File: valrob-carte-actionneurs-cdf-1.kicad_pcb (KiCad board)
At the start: 4 copper layers, 50 x 50 mm, 126 parts, among them J1 USB_C_Receptacle_USB2.0_14P, J2 Conn_01x02, J3 Conn_01x02, J4 Conn_01x04_Pin, J5 Conn_01x02, J6 Conn_01x02, J7 Conn_01x12, M1 Motor_Servo, M10 Motor_Servo, M11 Motor_Servo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

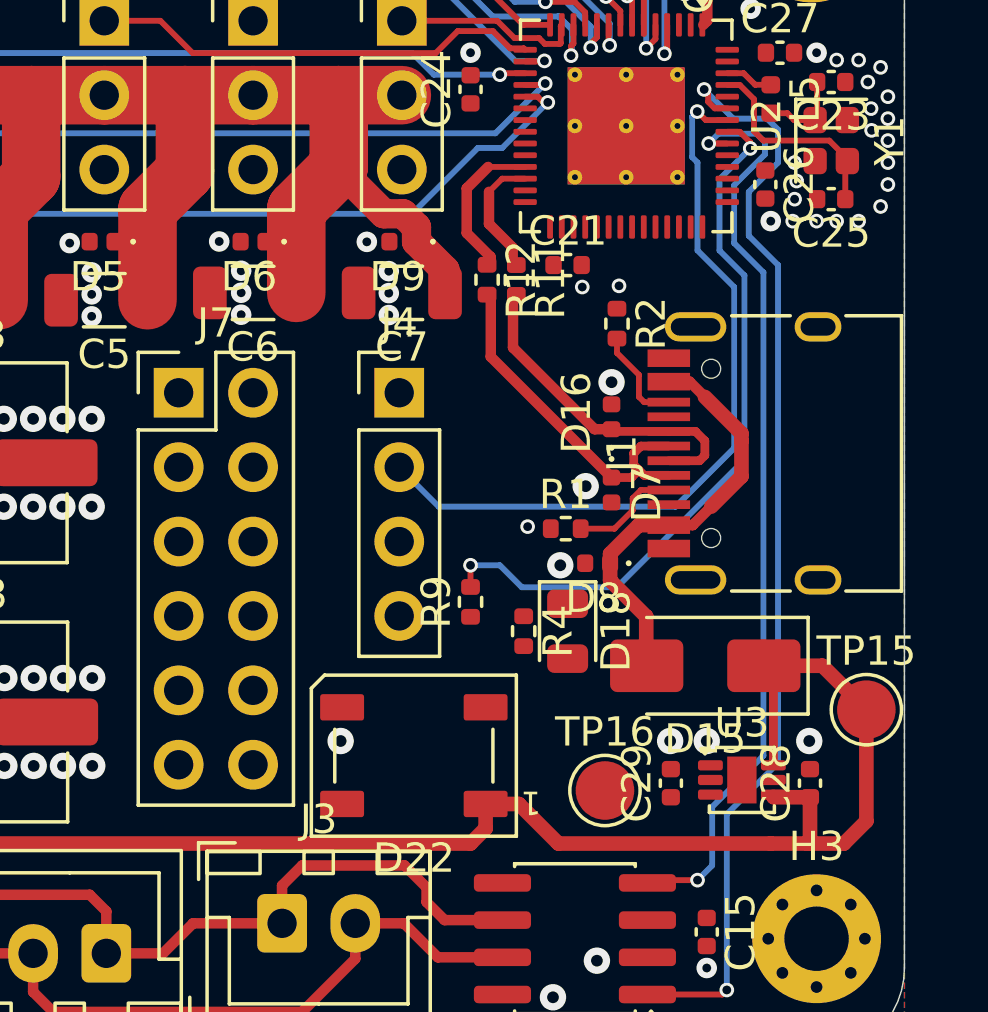
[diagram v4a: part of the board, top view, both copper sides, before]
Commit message: pcb: add spare GPIOs routing
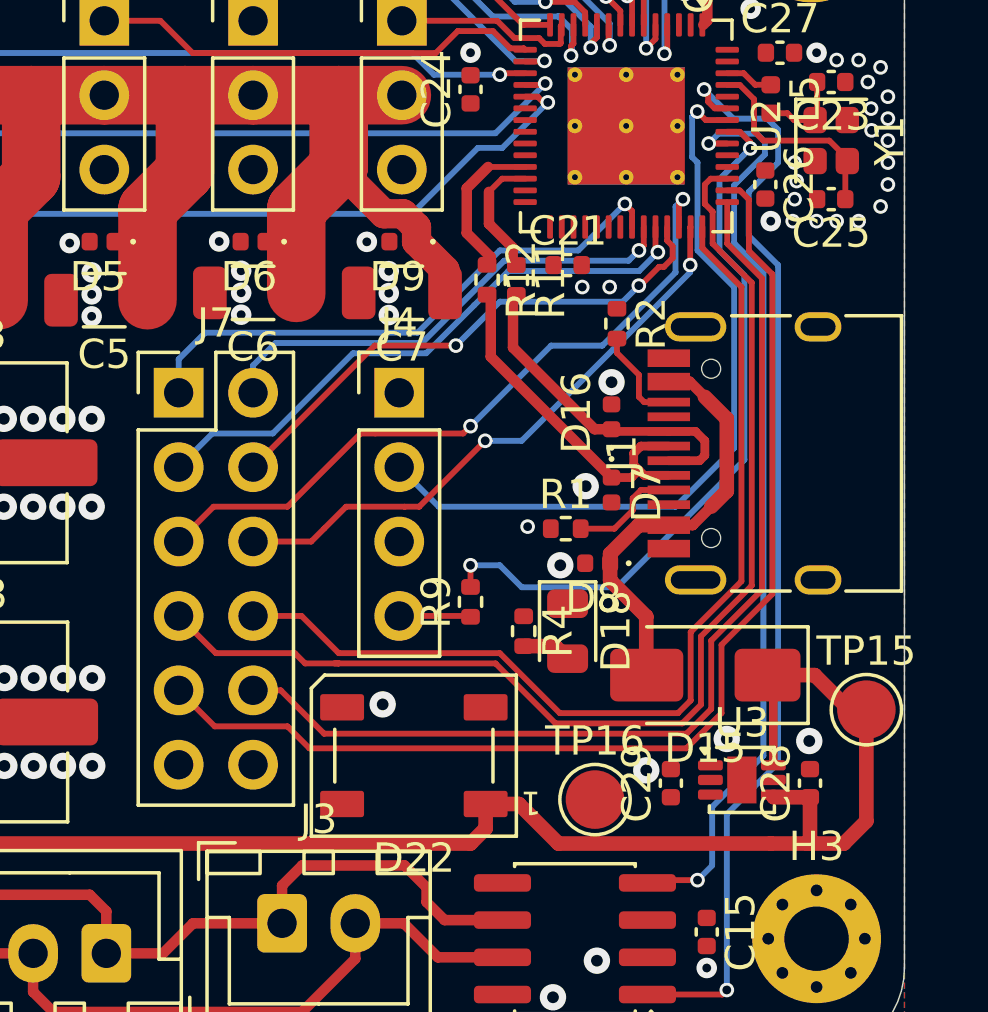
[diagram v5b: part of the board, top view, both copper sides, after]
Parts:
- moved TP16 0.46 mm to (123.4, 100.2)
- moved D15 0.32 mm to (127.2, 96.0)
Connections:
- J7 pad 10: /GPIO40 -> /GPIO38
- J7 pad 11: /GPIO41 -> +3V3
- J7 pad 7: /GPIO37 -> /GPIO40
- J7 pad 8: /GPIO38 -> /GPIO37
- U2 pad 47: /GPIO41 -> unconnected-(U2-MTDI/JTAG/GPIO41-Pad47)
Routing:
- net /GPIO40: track 0.00 -> 39.8 mm
- net /GPIO39: track 0.00 -> 39.3 mm
- net /GPIO38: track 0.00 -> 35.1 mm
- net /GPIO37: track 0.00 -> 33.9 mm
- net /GPIO35: track 0.00 -> 24.4 mm, vias 0 -> 2
- net /GPIO33: track 0.00 -> 20.3 mm, vias 0 -> 1
- net /GPIO36: track 0.00 -> 20.3 mm, vias 0 -> 2
- net /GPIO48: track 0.00 -> 19.5 mm, vias 0 -> 1
- net /GPIO34: track 0.00 -> 18.4 mm, vias 0 -> 2
- net /GPIO47: track 0.00 -> 16.6 mm, vias 0 -> 1
- net Net-(J4-Pin_4): track 0.00 -> 2.45 mm
- net Net-(D18-A): track 0.00 -> 1.68 mm

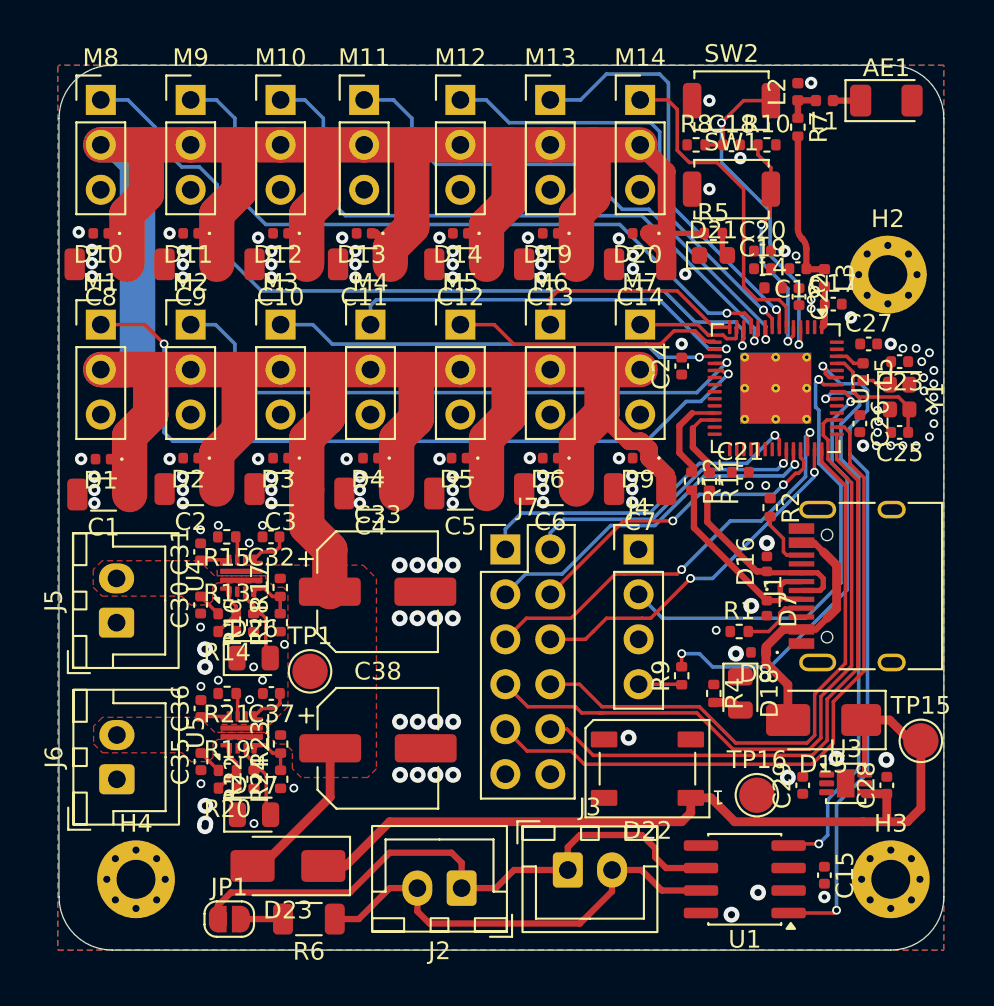
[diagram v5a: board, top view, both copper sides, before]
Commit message: pcb: add efuse mcu routing
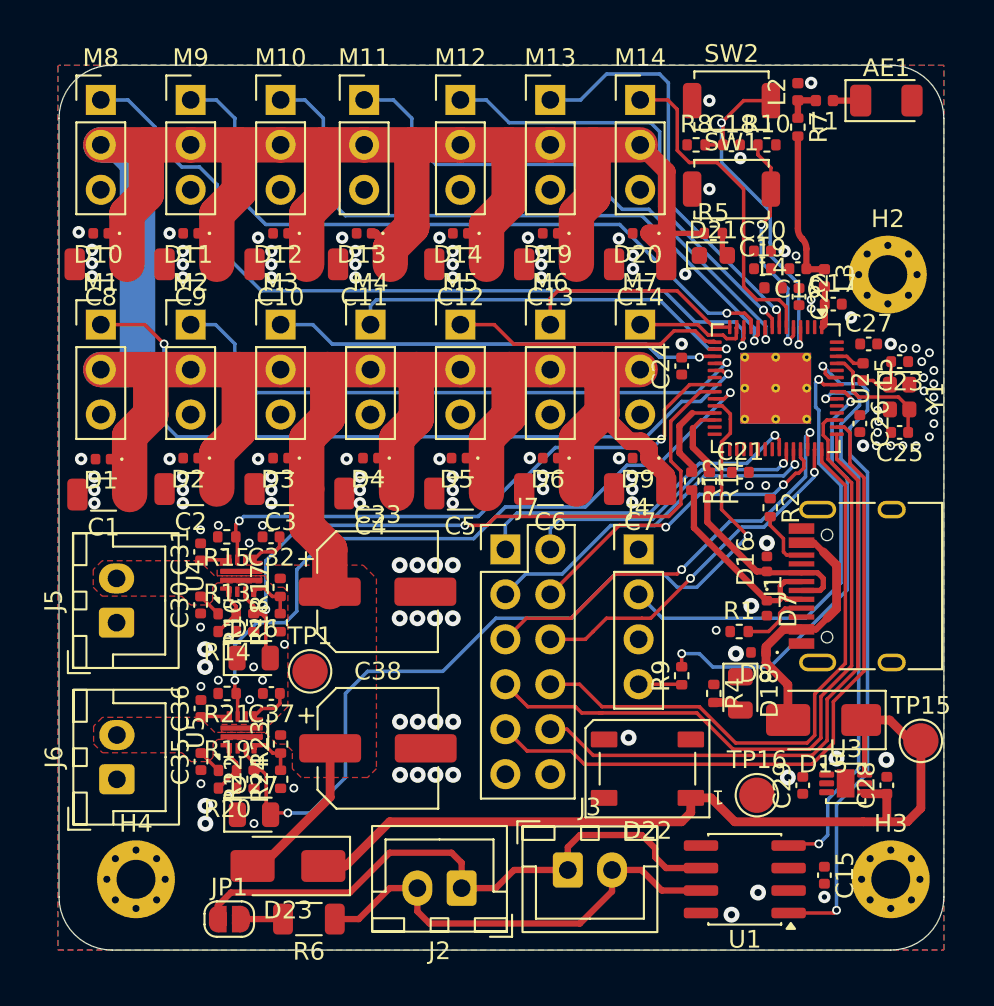
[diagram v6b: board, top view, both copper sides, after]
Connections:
- U2 pad 21: /PG_B -> /ILM_B
- U2 pad 22: /PG_A -> /PG_B
- U2 pad 24: /ILM_B -> /PG_A
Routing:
- net /PG_A: track 4.58 -> 50.3 mm, vias 0 -> 2
- net /ILM_A: track 1.34 -> 40.4 mm, vias 0 -> 2
- net /PG_B: track 4.58 -> 41.5 mm, vias 0 -> 2
- net /ILM_B: track 1.34 -> 33.2 mm, vias 0 -> 2
- net /SERVO1: track 43.6 -> 43.1 mm
- net GND: vias 137 -> 135

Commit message: pcb: add RGB led routing
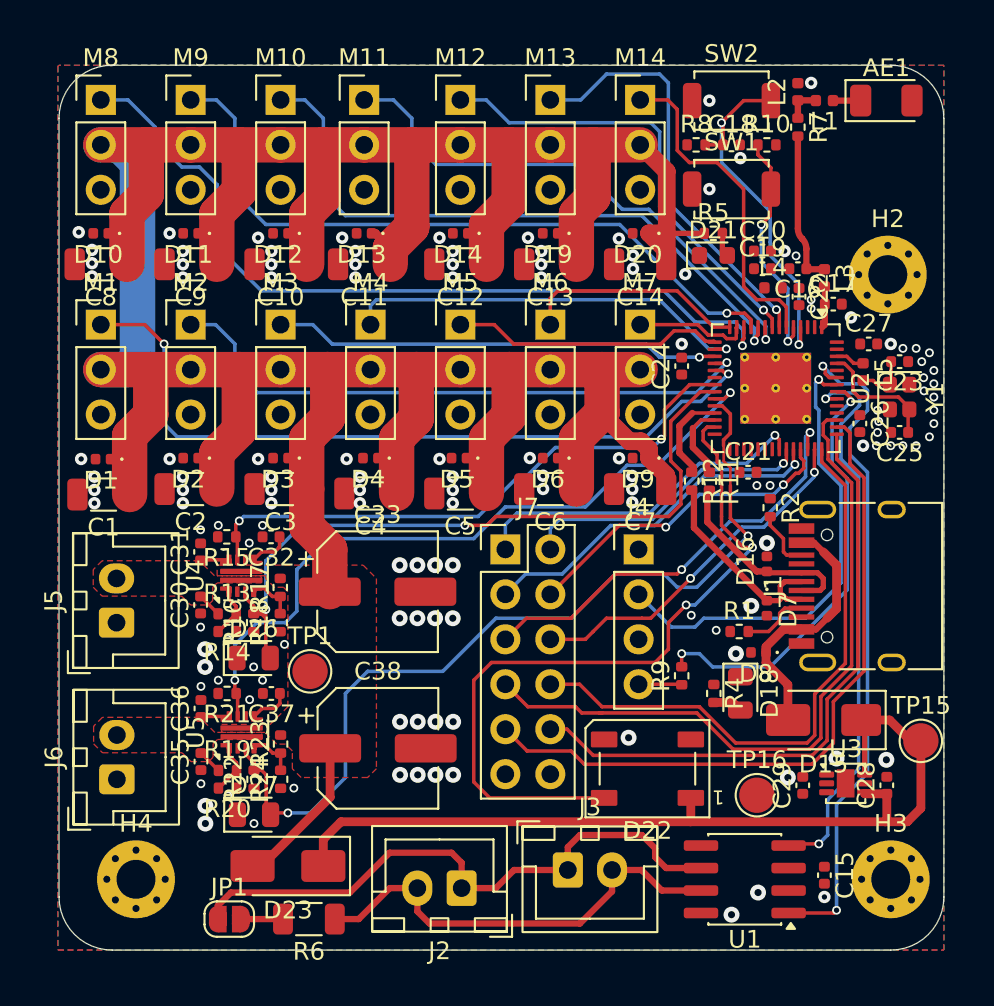
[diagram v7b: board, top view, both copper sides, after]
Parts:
- moved C21 0.44 mm to (122.9, 82.0)
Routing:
- net /RGB: track 0.00 -> 42.0 mm, vias 0 -> 2
- net +5V_MCU: track 50.9 -> 51.6 mm
- net GND: vias 135 -> 136

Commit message: pcb: add 3v3 pwr routing
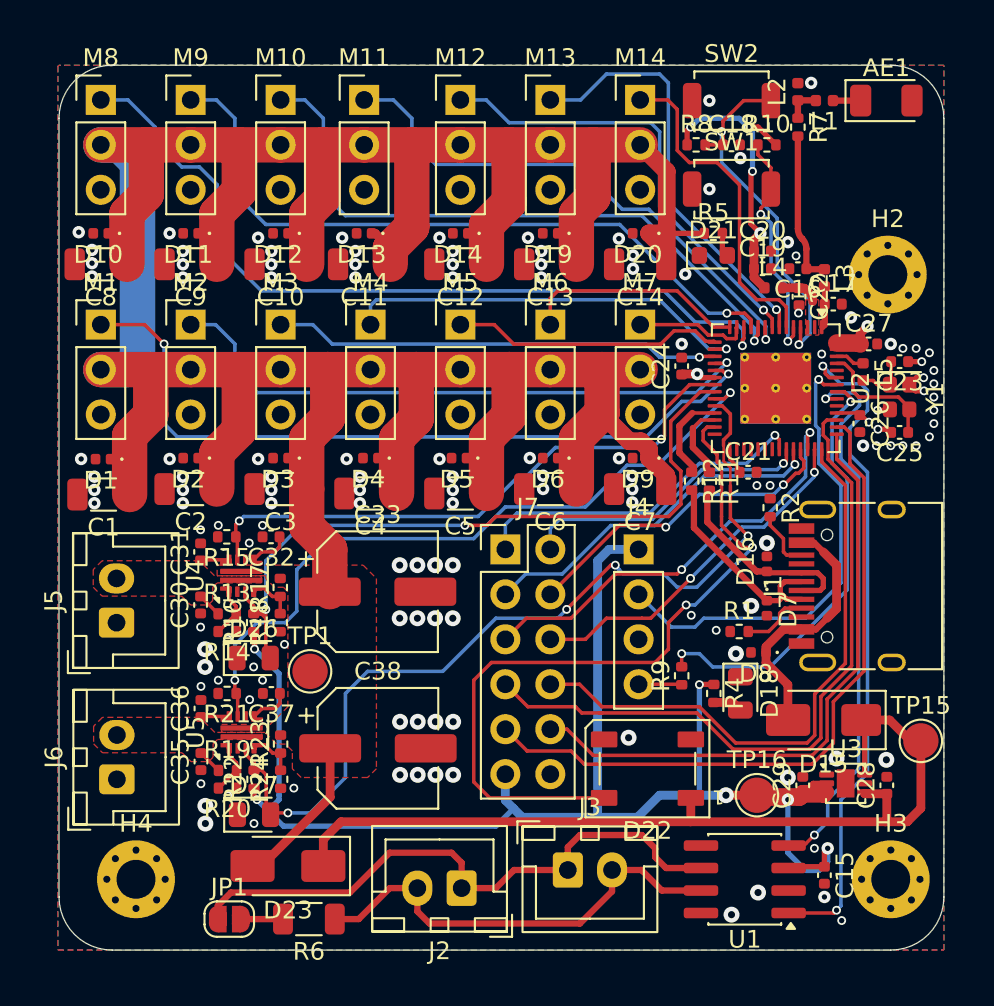
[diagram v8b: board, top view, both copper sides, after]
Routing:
- net +3V3: track 0.00 -> 146.1 mm, vias 0 -> 13
- net GND: track 0.00 -> 4.26 mm, vias 136 -> 137
- net VDD3P3: track 0.00 -> 2.26 mm
- net /VDD_SPI: track 0.00 -> 1.53 mm
- net /BOOT: track 13.2 -> 14.2 mm
- net /PG_A: track 50.2 -> 50.8 mm, vias 2 -> 4
- added copper zone on F.Cu, net VDD3P3
